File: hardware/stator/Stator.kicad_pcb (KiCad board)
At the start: 2 copper layers, 200 x 200 mm, 1 part

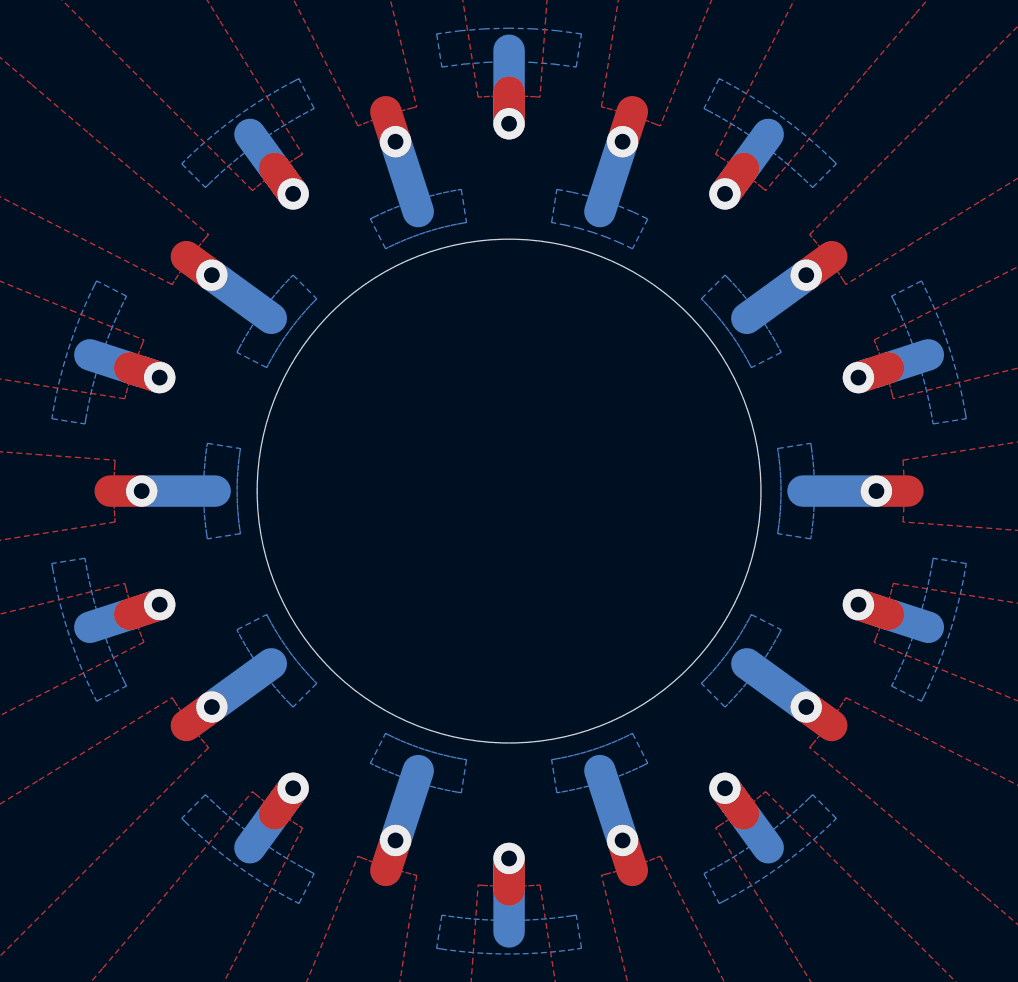
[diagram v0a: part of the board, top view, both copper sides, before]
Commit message: TENG layout
Updated the TENG layout.
Increased the hub gap area for both layouts.
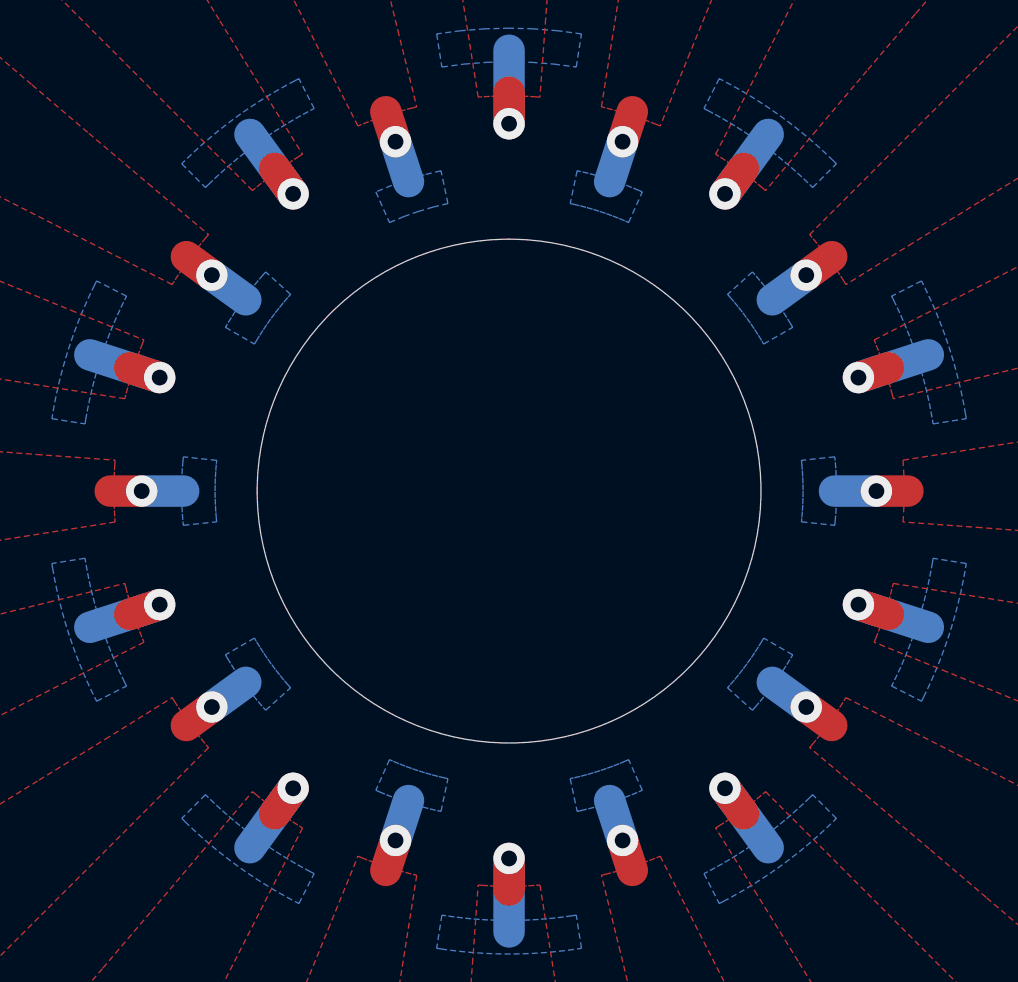
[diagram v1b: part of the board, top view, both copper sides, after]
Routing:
- net A: track 50.0 -> 15.0 mm
